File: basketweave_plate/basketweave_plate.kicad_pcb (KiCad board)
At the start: 2 copper layers, 371.5 x 119.1 mm, 1 part

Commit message: changed logo, name, and pattern design
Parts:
- removed the G*** at (64.7, 140.3)
- added G***: LOGO, basketweave_plate:logo_plate, B.Cu at (87.3, 130.2)
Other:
- outline, holes or cut-outs redrawn
- board text removed: "Designed by Noah L"
- board text removed: "JLCJLCJLCJLC"

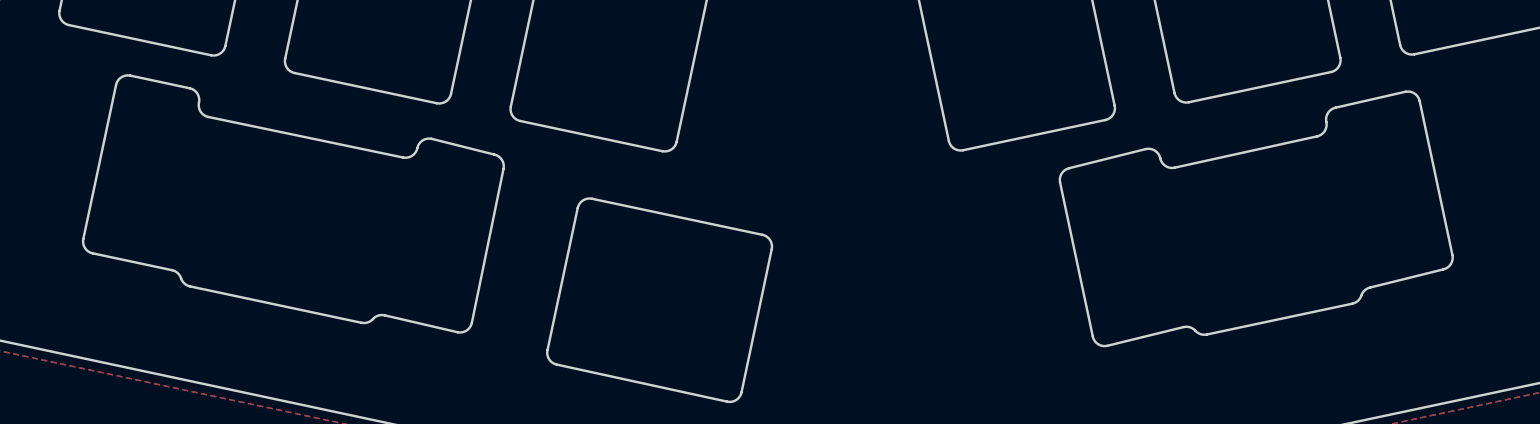
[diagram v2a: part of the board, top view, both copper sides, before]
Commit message: fixed inaccurate label
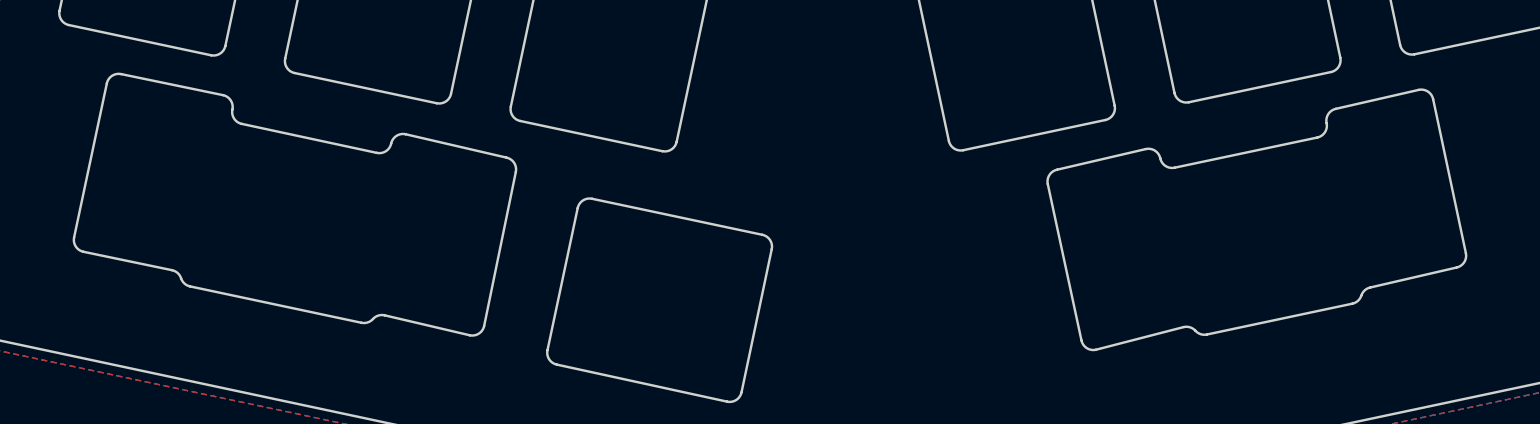
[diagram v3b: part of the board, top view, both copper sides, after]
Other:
- outline, holes or cut-outs redrawn
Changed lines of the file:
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@@
   (gr_line (start 262.550733 126.213914) (end 274.308691 123.72975) (layer Edge.Cuts) (width 0.2))
   (gr_arc (start 223.127232 147.182058) (end 223.870377 146.512927) (angle -60) (layer Edge.Cuts) (width 0.2))
-  (gr_arc (start 216.374249 146.778756) (end 215.396102 146.986669) (angle -90) (layer Edge.Cuts) (width 0.2))
+  (gr_arc (start 215.438087 147.103853) (end 214.45994 147.311766) (angle -90) (layer Edge.Cuts) (width 0.2))
   (gr_line (start 264.275437 139.137745) (end 261.780497 127.399974) (layer Edge.Cuts) (width 0.2))
   (gr_line (start 185.199748 152.366756) (end 171.131956 149.306356) (layer Edge.Cuts) (width 0.2))
   (gr_arc (start 139.152879 142.489215) (end 140.103936 142.180198) (angle -60) (layer Edge.Cuts) (width 0.2))
-  (gr_arc (start 235.6604 129.066989) (end 235.452488 128.08884) (angle -90) (layer Edge.Cuts) (width 0.2))
+  (gr_arc (start 235.682387 129.162028) (end 235.474475 128.183879) (angle -90) (layer Edge.Cuts) (width 0.2))
   (gr_arc (start 173.834807 136.590438) (end 174.042718 135.61229) (angle -90) (layer Edge.Cuts) (width 0.2))
   (gr_line (start 188.88075 139.77481) (end 186.385808 151.59652) (layer Edge.Cuts) (width 0.2))
@@
   (gr_arc (start 171.339867 148.328209) (end 170.36172 148.120298) (angle -90) (layer Edge.Cuts) (width 0.2))
   (gr_arc (start 277.011543 136.445667) (end 277.219454 137.423814) (angle -90) (layer Edge.Cuts) (width 0.2))
-  (gr_line (start 245.093662 140.263905) (end 242.39081 127.547986) (layer Edge.Cuts) (width 0.2))
+  (gr_line (start 246.204912 140.105155) (end 243.50206 127.389236) (layer Edge.Cuts) (width 0.2))
   (gr_line (start 275.49475 124.499985) (end 277.98969 136.237756) (layer Edge.Cuts) (width 0.2))
   (gr_arc (start 262.758644 127.192062) (end 262.550733 126.213914) (angle -90) (layer Edge.Cuts) (width 0.2))
@@
   (gr_arc (start 141.054991 141.871181) (end 140.103936 142.180198) (angle -60) (layer Edge.Cuts) (width 0.2))
   (gr_arc (start 224.613521 145.843797) (end 223.870377 146.512927) (angle -60) (layer Edge.Cuts) (width 0.2))
-  (gr_arc (start 163.137602 145.653518) (end 162.92969 146.631666) (angle -90) (layer Edge.Cuts) (width 0.2))
-  (gr_arc (start 213.671398 134.062838) (end 213.463486 133.084691) (angle -90) (layer Edge.Cuts) (width 0.2))
-  (gr_arc (start 140.602884 127.462313) (end 141.581031 127.670225) (angle -90) (layer Edge.Cuts) (width 0.2))
-  (gr_line (start 215.396102 146.986669) (end 212.69325 134.27075) (layer Edge.Cuts) (width 0.2))
-  (gr_line (start 216.582162 147.756903) (end 222.91932 146.20391) (layer Edge.Cuts) (width 0.2))
-  (gr_arc (start 133.009294 139.138673) (end 132.031146 138.930762) (angle -90) (layer Edge.Cuts) (width 0.2))
-  (gr_line (start 235.452488 128.08884) (end 241.20475 126.77775) (layer Edge.Cuts) (width 0.2))
-  (gr_line (start 162.92969 146.631666) (end 156.899964 145.234235) (layer Edge.Cuts) (width 0.2))
-  (gr_arc (start 158.634103 131.225031) (end 158.426191 132.203179) (angle -90) (layer Edge.Cuts) (width 0.2))
+  (gr_arc (start 164.153602 145.907518) (end 163.94569 146.885666) (angle -90) (layer Edge.Cuts) (width 0.2))
+  (gr_arc (start 212.655398 134.189838) (end 212.447486 133.211691) (angle -90) (layer Edge.Cuts) (width 0.2))
+  (gr_arc (start 143.365134 128.033813) (end 144.343281 128.241725) (angle -90) (layer Edge.Cuts) (width 0.2))
+  (gr_line (start 214.45994 147.311766) (end 211.67725 134.39775) (layer Edge.Cuts) (width 0.2))
+  (gr_line (start 215.646 148.082) (end 222.91932 146.20391) (layer Edge.Cuts) (width 0.2))
+  (gr_arc (start 132.247294 139.011673) (end 131.269146 138.803762) (angle -90) (layer Edge.Cuts) (width 0.2))
+  (gr_line (start 235.474475 128.183879) (end 242.316 126.619) (layer Edge.Cuts) (width 0.2))
+  (gr_line (start 163.94569 146.885666) (end 156.899964 145.234235) (layer Edge.Cuts) (width 0.2))
+  (gr_arc (start 156.475103 130.844031) (end 156.267191 131.822179) (angle -90) (layer Edge.Cuts) (width 0.2))
   (gr_arc (start 238.523411 143.916646) (end 238.3155 142.9385) (angle -60) (layer Edge.Cuts) (width 0.2))
-  (gr_line (start 140.810795 126.484165) (end 135.920057 125.444607) (layer Edge.Cuts) (width 0.2))
-  (gr_line (start 238.3155 142.9385) (end 244.323425 141.449966) (layer Edge.Cuts) (width 0.2))
+  (gr_line (start 143.573046 127.055666) (end 135.158057 125.317607) (layer Edge.Cuts) (width 0.2))
+  (gr_line (start 238.3155 142.9385) (end 245.434675 141.291216) (layer Edge.Cuts) (width 0.2))
   (gr_arc (start 156.692053 146.212381) (end 156.899964 145.234235) (angle -60) (layer Edge.Cuts) (width 0.2))
-  (gr_line (start 132.801382 140.116821) (end 139.360791 141.511067) (layer Edge.Cuts) (width 0.2))
+  (gr_line (start 132.039383 139.989821) (end 139.360791 141.511067) (layer Edge.Cuts) (width 0.2))
   (gr_arc (start 155.205763 144.874121) (end 154.997851 145.852269) (angle -60) (layer Edge.Cuts) (width 0.2))
-  (gr_arc (start 241.412662 127.755898) (end 242.39081 127.547986) (angle -90) (layer Edge.Cuts) (width 0.2))
-  (gr_arc (start 165.752817 132.9376) (end 166.730965 133.145511) (angle -90) (layer Edge.Cuts) (width 0.2))
+  (gr_arc (start 242.523912 127.597148) (end 243.50206 127.389236) (angle -90) (layer Edge.Cuts) (width 0.2))
+  (gr_arc (start 166.768817 133.1916) (end 167.746965 133.399511) (angle -90) (layer Edge.Cuts) (width 0.2))
   (gr_line (start 154.997851 145.852269) (end 140.84708 142.849328) (layer Edge.Cuts) (width 0.2))
-  (gr_line (start 132.031146 138.930762) (end 134.733998 126.214843) (layer Edge.Cuts) (width 0.2))
-  (gr_line (start 222.155094 133.045853) (end 233.912016 130.460961) (layer Edge.Cuts) (width 0.2))
-  (gr_arc (start 233.704105 129.482812) (end 233.912016 130.460961) (angle -90) (layer Edge.Cuts) (width 0.2))
+  (gr_line (start 131.269146 138.803762) (end 133.971998 126.087843) (layer Edge.Cuts) (width 0.2))
+  (gr_line (start 222.155094 133.045853) (end 233.934 130.556) (layer Edge.Cuts) (width 0.2))
+  (gr_arc (start 233.726089 129.577851) (end 233.934 130.556) (angle -90) (layer Edge.Cuts) (width 0.2))
   (gr_line (start 236.82921 144.276759) (end 224.821433 146.821944) (layer Edge.Cuts) (width 0.2))
-  (gr_line (start 165.960728 131.959452) (end 160.79831 130.662706) (layer Edge.Cuts) (width 0.2))
-  (gr_arc (start 135.712146 126.422755) (end 135.920057 125.444607) (angle -90) (layer Edge.Cuts) (width 0.2))
-  (gr_line (start 142.351267 128.856284) (end 158.426191 132.203179) (layer Edge.Cuts) (width 0.2))
-  (gr_line (start 164.11575 145.86143) (end 166.730965 133.145511) (layer Edge.Cuts) (width 0.2))
-  (gr_arc (start 244.115513 140.471817) (end 244.323425 141.449966) (angle -90) (layer Edge.Cuts) (width 0.2))
-  (gr_line (start 219.782974 131.505383) (end 213.463486 133.084691) (layer Edge.Cuts) (width 0.2))
-  (gr_arc (start 142.559179 127.878136) (end 141.581031 127.670225) (angle -90) (layer Edge.Cuts) (width 0.2))
-  (gr_arc (start 160.590398 131.640854) (end 160.79831 130.662706) (angle -90) (layer Edge.Cuts) (width 0.2))
+  (gr_line (start 166.976728 132.213452) (end 158.63931 130.281706) (layer Edge.Cuts) (width 0.2))
+  (gr_arc (start 134.950146 126.295755) (end 135.158057 125.317607) (angle -90) (layer Edge.Cuts) (width 0.2))
+  (gr_line (start 145.113518 129.427784) (end 156.267191 131.822179) (layer Edge.Cuts) (width 0.2))
+  (gr_line (start 165.13175 146.11543) (end 167.746965 133.399511) (layer Edge.Cuts) (width 0.2))
+  (gr_arc (start 245.226763 140.313067) (end 245.434675 141.291216) (angle -90) (layer Edge.Cuts) (width 0.2))
+  (gr_line (start 219.782974 131.505383) (end 212.447486 133.211691) (layer Edge.Cuts) (width 0.2))
+  (gr_arc (start 145.321429 128.449636) (end 144.343281 128.241725) (angle -90) (layer Edge.Cuts) (width 0.2))
+  (gr_arc (start 158.431398 131.259854) (end 158.63931 130.281706) (angle -90) (layer Edge.Cuts) (width 0.2))
   (gr_arc (start 168.312943 128.209228) (end 167.334796 128.001317) (angle -90) (layer Edge.Cuts) (width 0.2))
   (gr_line (start 370.09375 68.35625) (end 383.175 68.35625) (layer Edge.Cuts) (width 0.2))
